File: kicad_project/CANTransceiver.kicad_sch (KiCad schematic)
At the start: 19 parts, among them J10 1x2, J11 1x2, J9 1x2, M1 QPC02SXGN-RC, M2 QPC02SXGN-RC, U17 MCP2515-xST, U18 TJA1051T-3, U19 TJA1051T-3, X3 16.000MHz

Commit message: ERC passing!
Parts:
- added R45: 10k, Resistor_SMD:R_1206_3216Metric, symbol Device:R_US
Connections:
- net GND: now also R45.2
- net MCU_CAN_TX: now also R45.1
- net CAN_BUS renamed MCP_CAN_RX
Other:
- moved on the sheet: J9
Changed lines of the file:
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@@
 		(color 0 0 0 0)
 	)
+	(junction
+		(at 73.66 140.97)
+		(diameter 0)
+		(color 0 0 0 0)
+	)
 	(no_connect
 		(at 99.06 69.85)
@@
 	(wire
 		(pts
-			(xy 76.2 140.97) (xy 105.41 140.97)
+			(xy 72.39 140.97) (xy 73.66 140.97)
 		)
 		(stroke
@@
 	(wire
 		(pts
-			(xy 76.2 143.51) (xy 105.41 143.51)
+			(xy 72.39 143.51) (xy 105.41 143.51)
 		)
 		(stroke
@@
 		)
 	)
+	(wire
+		(pts
+			(xy 73.66 160.02) (xy 73.66 162.56)
+		)
+		(stroke
+			(width 0)
+			(type default)
+		)
+	)
 	(bus
 		(pts
@@
 	(wire
 		(pts
+			(xy 73.66 140.97) (xy 105.41 140.97)
+		)
+		(stroke
+			(width 0)
+			(type default)
+		)
+	)
+	(wire
+		(pts
 			(xy 53.34 85.09) (xy 53.34 74.93)
 		)
@@
 	(wire
 		(pts
+			(xy 73.66 140.97) (xy 73.66 152.4)
+		)
+		(stroke
+			(width 0)
+			(type default)
+		)
+	)
+	(wire
+		(pts
 			(xy 99.06 52.07) (xy 114.3 52.07)
 		)
@@
 		)
 	)
-	(label "SPI.SCLK"
-		(at 48.26 59.69 0)
+	(label "SPI.CAN_CS"
+		(at 48.26 57.15 0)
 		(effects
 			(font
@@
 		)
 	)
-	(label "SPI.CAN_CS"
-		(at 48.26 57.15 0)
+	(label "SPI.SCLK"
+		(at 48.26 59.69 0)
 		(effects
 			(font
@@
 		)
 	)
-	(hierarchical_label "CAN_BUS"
+	(hierarchical_label "MCP_CAN_RX"
 		(shape output)
 		(at 119.38 27.94 0)
@@
 	(symbol
 		(lib_id "Connector:Conn_01x02_Pin")
-		(at 71.12 140.97 0)
+		(at 67.31 140.97 0)
 		(unit 1)
 		(exclude_from_sim no)
@@
 		(fields_autoplaced yes)
 		(property "Reference" "J9"
-			(at 71.755 135.89 0)
+			(at 67.945 135.89 0)
 			(effects
 				(font
@@
 		)
 		(property "Value" "1x2"
-			(at 71.755 138.43 0)
+			(at 67.945 138.43 0)
 			(effects
 				(font
@@
 		)
 		(property "Footprint" "Connector_PinHeader_2.54mm:PinHeader_1x02_P2.54mm_Vertical"
-			(at 71.12 140.97 0)
+			(at 67.31 140.97 0)
 			(effects
 				(font
@@
 		)
 		(property "Datasheet" "~"
-			(at 71.12 140.97 0)
+			(at 67.31 140.97 0)
 			(effects
 				(font
@@
 		)
 		(property "Description" "Generic connector, single row, 01x02, script generated"
-			(at 71.12 140.97 0)
+			(at 67.31 140.97 0)
 			(effects
 				(font
@@
 		)
 		(property "LibRef" "HEADER_2x1"
-			(at 71.12 140.97 0)
+			(at 67.31 140.97 0)
 			(effects
 				(font
@@
 		)
 		(property "SKU" "732-5315-ND"
-			(at 71.12 140.97 0)
+			(at 67.31 140.97 0)
 			(effects
 				(font
@@
 		)
 		(property "Supplier" "Digi-Key"
-			(at 71.12 140.97 0)
+			(at 67.31 140.97 0)
 			(effects
 				(font
@@
 	)
 	(symbol
+		(lib_id "power:GND")
+		(at 73.66 162.56 0)
+		(unit 1)
+		(exclude_from_sim no)
+		(in_bom yes)
+		(on_board yes)
+		(dnp no)
+		(fields_autoplaced yes)
+		(property "Reference" "#PWR0107"
+			(at 73.66 168.91 0)
+			(effects
+				(font
+					(size 1.27 1.27)
+				)
+				(hide yes)
+			)
+		)
+		(property "Value" "GND"
+			(at 73.66 167.64 0)
+			(effects
+				(font
+					(size 1.27 1.27)
+				)
+			)
+		)
+		(property "Footprint" ""
+			(at 73.66 162.56 0)
+			(effects
+				(font
+					(size 1.27 1.27)
+				)
+				(hide yes)
+			)
+		)
+		(property "Datasheet" ""
+			(at 73.66 162.56 0)
+			(effects
+				(font
+					(size 1.27 1.27)
+				)
+				(hide yes)
+			)
+		)
+		(property "Description" "Power symbol creates a global label with name \"GND\" , ground"
+			(at 73.66 162.56 0)
+			(effects
+				(font
+					(size 1.27 1.27)
+				)
+				(hide yes)
+			)
+		)
+		(pin "1"
+		)
+		(instances
+			(project "mbed-ce-ci-shield-v2"
+				(path "/a0f40274-9469-4bcf-885c-e8b8a490ea54/6c93a008-184c-4fde-8753-4c70ee31e968"
+					(reference "#PWR0107")
+					(unit 1)
+				)
+			)
+		)
+	)
+	(symbol
 		(lib_id "Interface_CAN_LIN:MCP2515-xST")
 		(at 83.82 67.31 0)
@@
 			)
 		)
-		(property "Description" ""
+		(property "Description" "Resistor, US symbol"
 			(at 171.45 49.53 0)
 			(effects
@@
 			)
 		)
-		(property "Description" ""
+		(property "Description" "Resistor, US symbol"
 			(at 100.33 157.48 0)
 			(effects
@@
 			)
 		)
-		(property "Description" ""
+		(property "Description" "Unpolarized capacitor, small symbol"
 			(at 71.12 34.29 0)
 			(effects
@@
 	)
 	(symbol
+		(lib_id "Device:R_US")
+		(at 73.66 156.21 0)
+		(unit 1)
+		(exclude_from_sim no)
+		(in_bom yes)
+		(on_board yes)
+		(dnp no)
+		(fields_autoplaced yes)
+		(property "Reference" "R45"
+			(at 76.2 154.94 0)
+			(effects
+				(font
+					(size 1.27 1.27)
+				)
+				(justify left)
+			)
+		)
+		(property "Value" "10k"
+			(at 76.2 157.48 0)
+			(effects
+				(font
+					(size 1.27 1.27)
+				)
+				(justify left)
+			)
+		)
+		(property "Footprint" "Resistor_SMD:R_1206_3216Metric"
+			(at 74.676 156.464 90)
+			(effects
+				(font
+					(size 1.27 1.27)
+				)
+				(hide yes)
+			)
+		)
+		(property "Datasheet" "~"
+			(at 73.66 156.21 0)
+			(effects
+				(font
+					(size 1.27 1.27)
+				)
+				(hide yes)
+			)
+		)
+		(property "Description" "Resistor, US symbol"
+			(at 73.66 156.21 0)
+			(effects
+				(font
+					(size 1.27 1.27)
+				)
+				(hide yes)
+			)
+		)
+		(property "Supplier" "Digi-Key"
+			(at 73.66 156.21 0)
+			(effects
+				(font
+					(size 1.27 1.27)
+				)
+				(hide yes)
+			)
+		)
+		(property "LibRef" "ERJ-8ENF1002V"
+			(at 73.66 156.21 0)
+			(effects
+				(font
+					(size 1.27 1.27)
+				)
+				(hide yes)
+			)
+		)
+		(property "SKU" "P10.0KFCT-ND"
+			(at 73.66 156.21 0)
+			(effects
+				(font
+					(size 1.27 1.27)
+				)
+				(hide yes)
+			)
+		)
+		(pin "1"
+		)
+		(pin "2"
+		)
+		(instances
+			(project "mbed-ce-ci-shield-v2"
+				(path "/a0f40274-9469-4bcf-885c-e8b8a490ea54/6c93a008-184c-4fde-8753-4c70ee31e968"
+					(reference "R45")
+					(unit 1)
+				)
+			)
+		)
+	)
+	(symbol
 		(lib_id "power:+3.3V")
 		(at 38.1 68.58 0)
@@
 			)
 		)
-		(property "Description" ""
+		(property "Description" "Resistor, US symbol"
 			(at 121.92 68.58 0)
 			(effects
@@
 			)
 		)
-		(property "Description" ""
+		(property "Description" "Resistor, US symbol"
 			(at 171.45 156.21 0)
 			(effects
@@
 			)
 		)
-		(property "Description" ""
+		(property "Description" "Unpolarized capacitor, small symbol"
 			(at 128.27 38.1 0)
 			(effects
@@
 			)
 		)
-		(property "Description" ""
+		(property "Description" "Unpolarized capacitor, small symbol"
 			(at 109.22 125.73 0)
 			(effects
@@
 			)
 		)
-		(property "Description" ""
+		(property "Description" "Unpolarized capacitor, small symbol"
 			(at 90.17 157.48 0)
 			(effects
@@
 			)
 		)
-		(property "Description" "12 MHz HCMOS Oscillator 3.3V 4-SMD"
+		(property "Description" "3.3V HCMOS SMD Crystal Clock Oscillator, Abracon"
 			(at 38.1 85.09 0)
 			(effects
@@
 			)
 		)
-		(property "Description" ""
+		(property "Description" "Unpolarized capacitor, small symbol"
 			(at 114.3 66.04 0)
 			(effects
@@
 			)
 		)
-		(property "Description" ""
+		(property "Description" "Unpolarized capacitor, small symbol"
 			(at 19.05 83.82 0)
 			(effects

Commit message: Cleanups and more documentation
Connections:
- net CANH: now also J10.1 (Pin_1), R32.1, R44.2, U18.7 (CANH); no longer J11.2 (Pin_2), R32.2, R44.1, U18.6 (CANL)
- net CANL: now also J11.2 (Pin_2), R32.2, R44.1, U18.6 (CANL); no longer J10.1 (Pin_1), R32.1, R44.2, U18.7 (CANH)
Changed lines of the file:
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@@
 	(title_block
 		(title "CAN Transceiver")
+		(comment 1 "for the MCU to use.")
+		(comment 2 "Miniature CAN bus with an SPI-CAN adapter and a second CAN PHY")
 	)
 	(junction
@@
 		)
 	)
-	(label "CANH"
-		(at 177.8 62.23 270)
-		(effects
-			(font
-				(size 1.27 1.27)
-			)
-			(justify right bottom)
-		)
-	)
 	(label "MCU_CAN_TX"
 		(at 81.28 140.97 0)
@@
 		)
 	)
+	(label "CANH"
+		(at 166.37 73.66 270)
+		(effects
+			(font
+				(size 1.27 1.27)
+			)
+			(justify right bottom)
+		)
+	)
 	(label "CANL"
-		(at 166.37 62.23 270)
-		(effects
-			(font
+		(at 177.8 73.66 270)
+		(effects
+			(font

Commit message: Kate's suggestions, part 1
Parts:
- removed C27: 100nF, Capacitor_SMD:C_1206_3216Metric, symbol Device:C_Small
- removed X3: 16.000MHz, Oscillator:Oscillator_SMD_Abracon_ASV-4Pin_7.0x5.1mm, symbol Oscillator:ASV-xxxMHz
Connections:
- net CANH: no longer R44.2
- net CANL: no longer R44.1
- net 12MHZ_CLK: now reaches U17.9 (OSC1)
- net at J11.1 (Pin_1): no longer U19.6 (CANL)
- net at J10.2 (Pin_2), U19.7 (CANH): now also R44.2
- new net: R44.1, U19.6 (CANL)
- no-connect marks 9 -> 8
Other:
- moved on the sheet: J10, J11, M1, M2

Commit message: Finish new SD card schematic, ERC passing!
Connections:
- net at J11.1 (Pin_1): now also R44.1, U19.6 (CANL)
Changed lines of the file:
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@@
 	(wire
 		(pts
-			(xy 177.8 144.78) (xy 177.8 148.59)
+			(xy 111.76 54.61) (xy 111.76 57.15)
 		)
 		(stroke
@@
 	(wire
 		(pts
-			(xy 111.76 54.61) (xy 111.76 57.15)
+			(xy 177.8 143.51) (xy 177.8 148.59)
 		)
 		(stroke

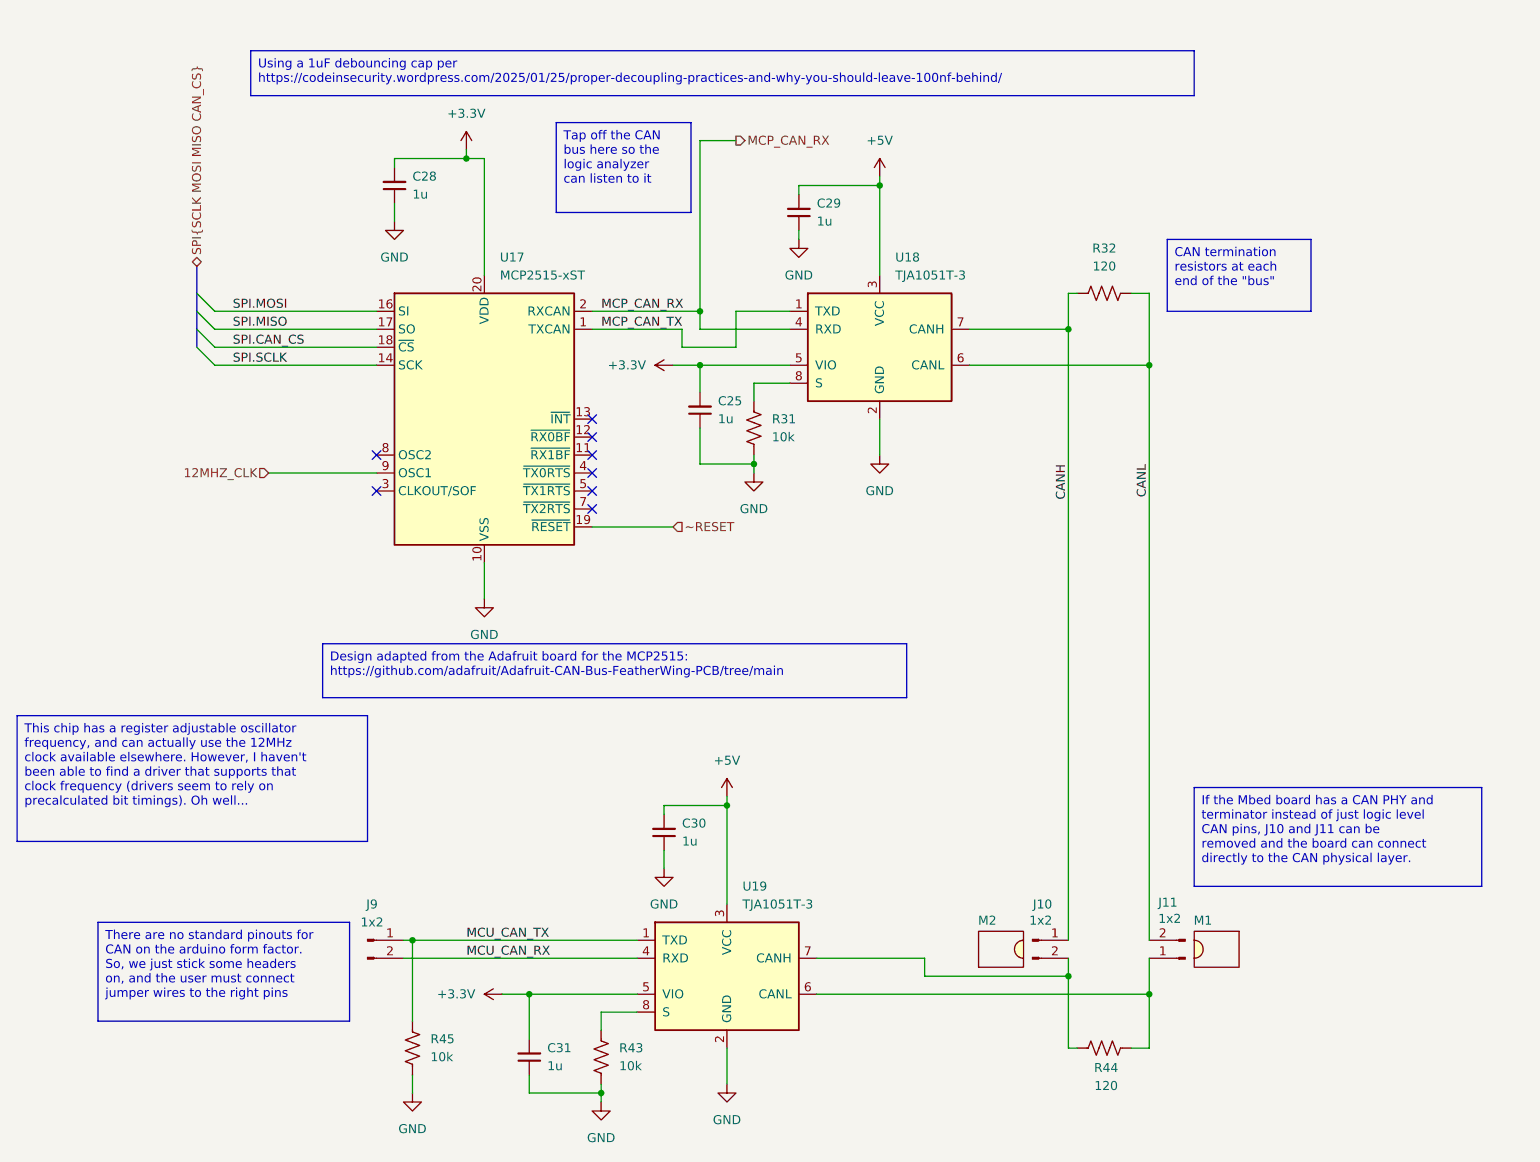
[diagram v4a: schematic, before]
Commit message: Switch out multiplexer, start switch FX2LP out for RP2040
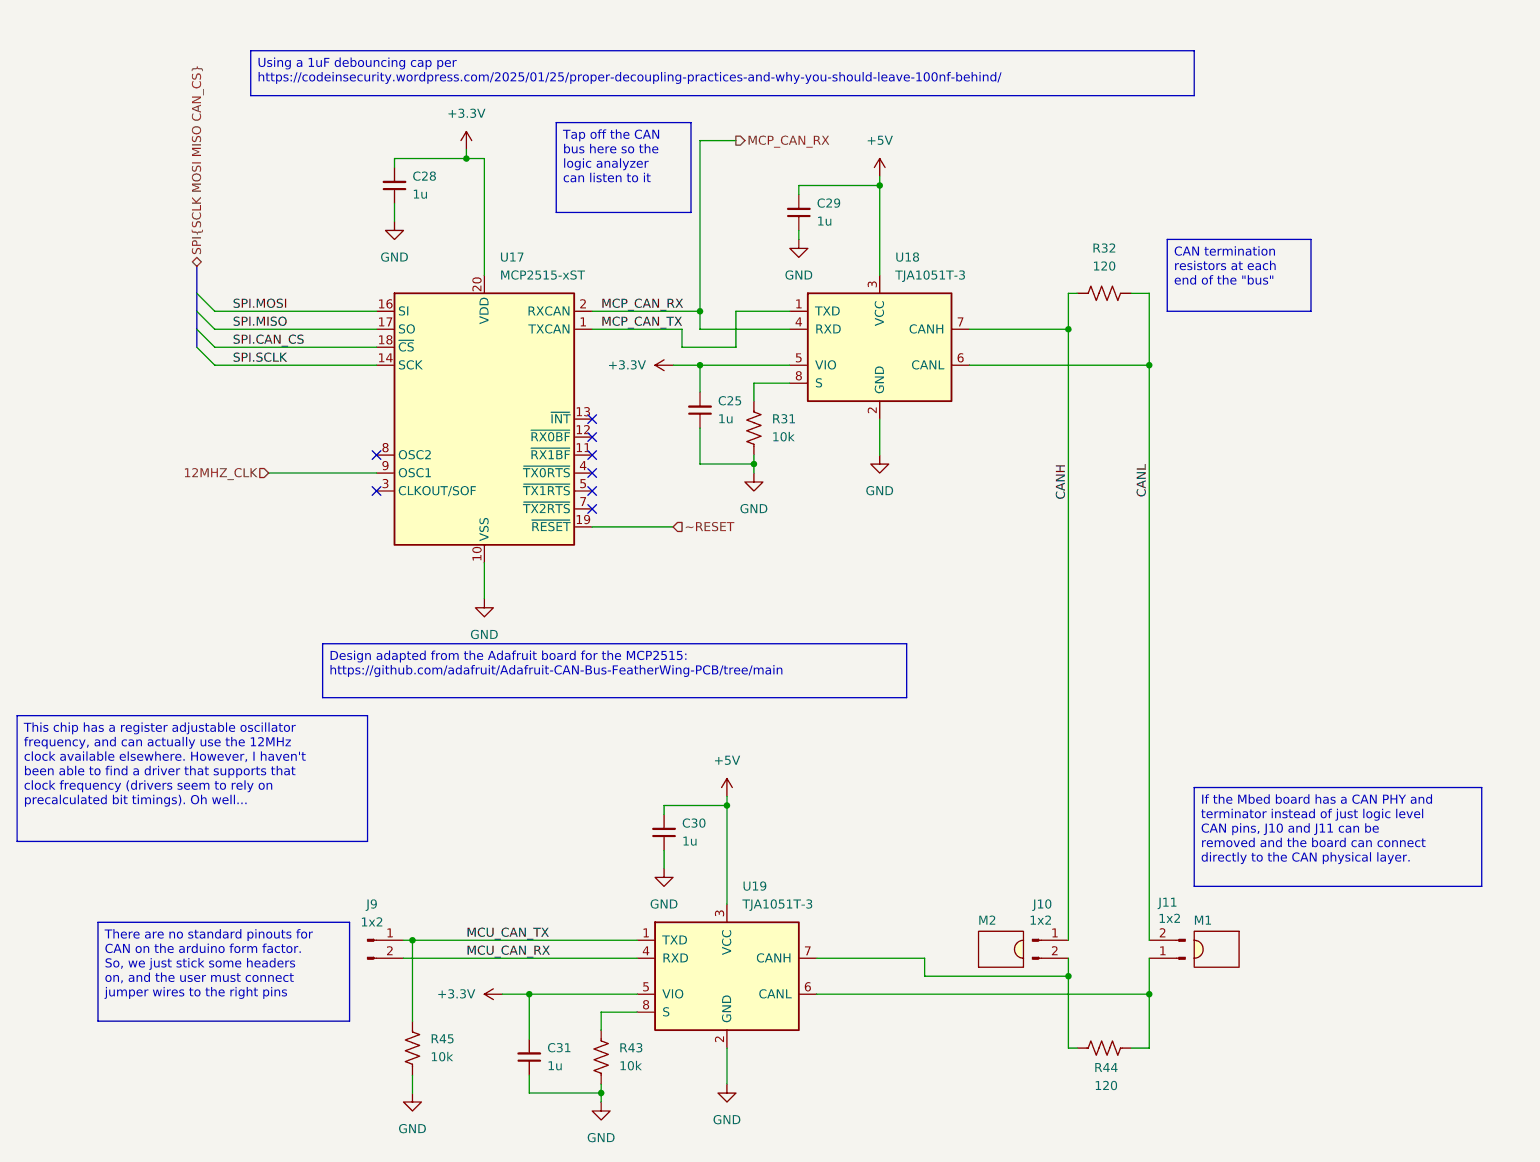
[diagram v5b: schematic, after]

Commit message: Fix some issues with rev 3 built PCB
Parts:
- U18, U19: footprint Package_SO:SOIC-8_3.9x4.9mm_P1.27mm -> project libraries:SOIC-8_3.9x4.9mm_P1.27mm_TJA1051T-3
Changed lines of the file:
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@@
 			)
 		)
-		(property "Footprint" "Package_SO:SOIC-8_3.9x4.9mm_P1.27mm"
+		(property "Footprint" "project libraries:SOIC-8_3.9x4.9mm_P1.27mm_TJA1051T-3"
 			(at 118.11 158.75 0)
 			(effects
@@
 			)
 		)
-		(property "Footprint" "Package_SO:SOIC-8_3.9x4.9mm_P1.27mm"
+		(property "Footprint" "project libraries:SOIC-8_3.9x4.9mm_P1.27mm_TJA1051T-3"
 			(at 139.7 69.85 0)
 			(effects
